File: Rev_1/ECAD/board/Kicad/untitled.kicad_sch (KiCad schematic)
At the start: 1 part

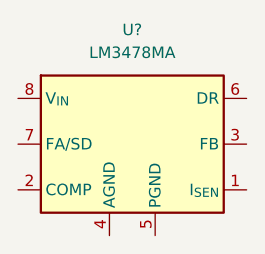
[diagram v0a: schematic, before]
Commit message: Moved Input Capacitors to minimize loop area and created pours for boost converter
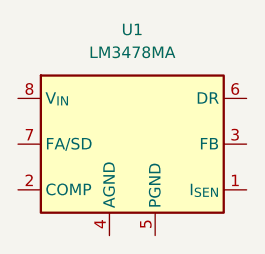
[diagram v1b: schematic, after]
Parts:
- gave numbers to parts that had none: 1
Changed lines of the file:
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@@
 		(dnp no)
 		(fields_autoplaced yes)
-		(property "Reference" "U?"
+		(property "Reference" "U1"
 			(at 64.77 38.1 0)
 			(effects
@@
 			(project ""
 				(path "/bb89802d-7e38-4fba-a75e-923c723cd6a1/ac666ba1-6694-41e5-b795-864ebc43cc42"
-					(reference "U?")
+					(reference "U1")
 					(unit 1)
 				)

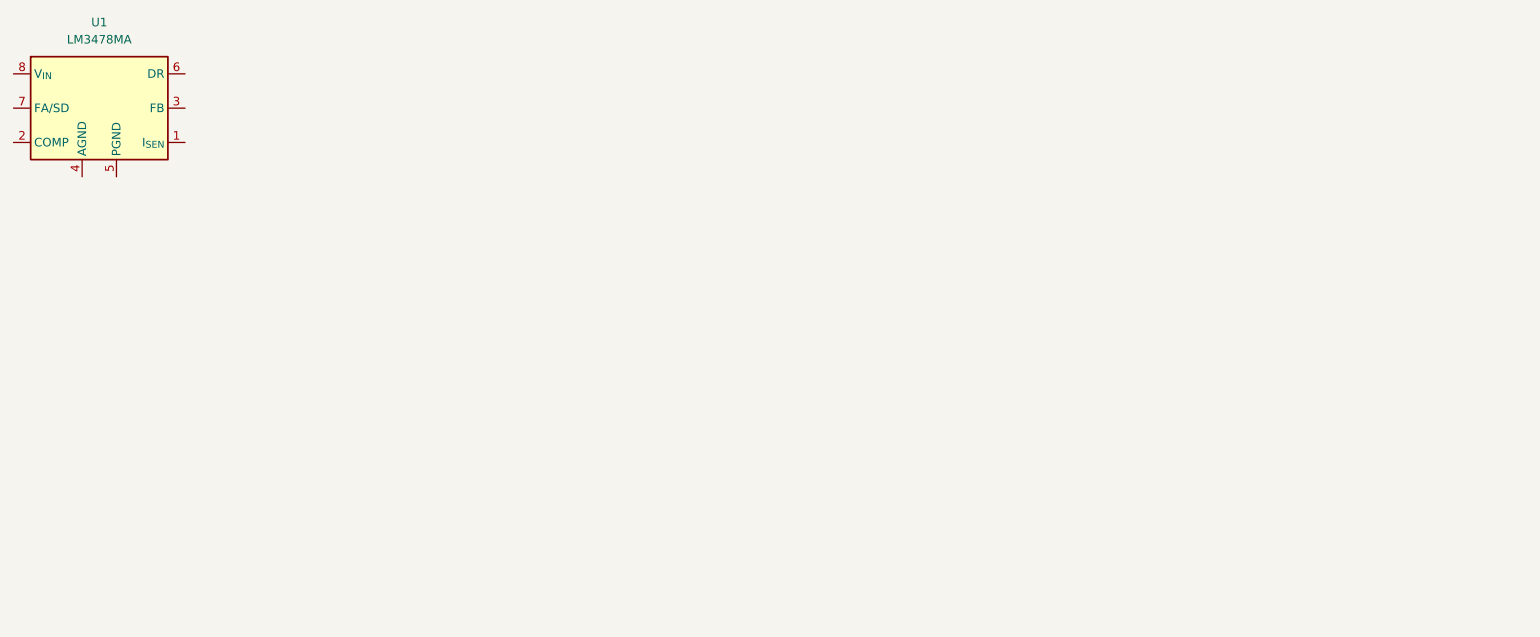
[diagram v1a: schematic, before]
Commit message: Added inverted buck-boost for -17V rail
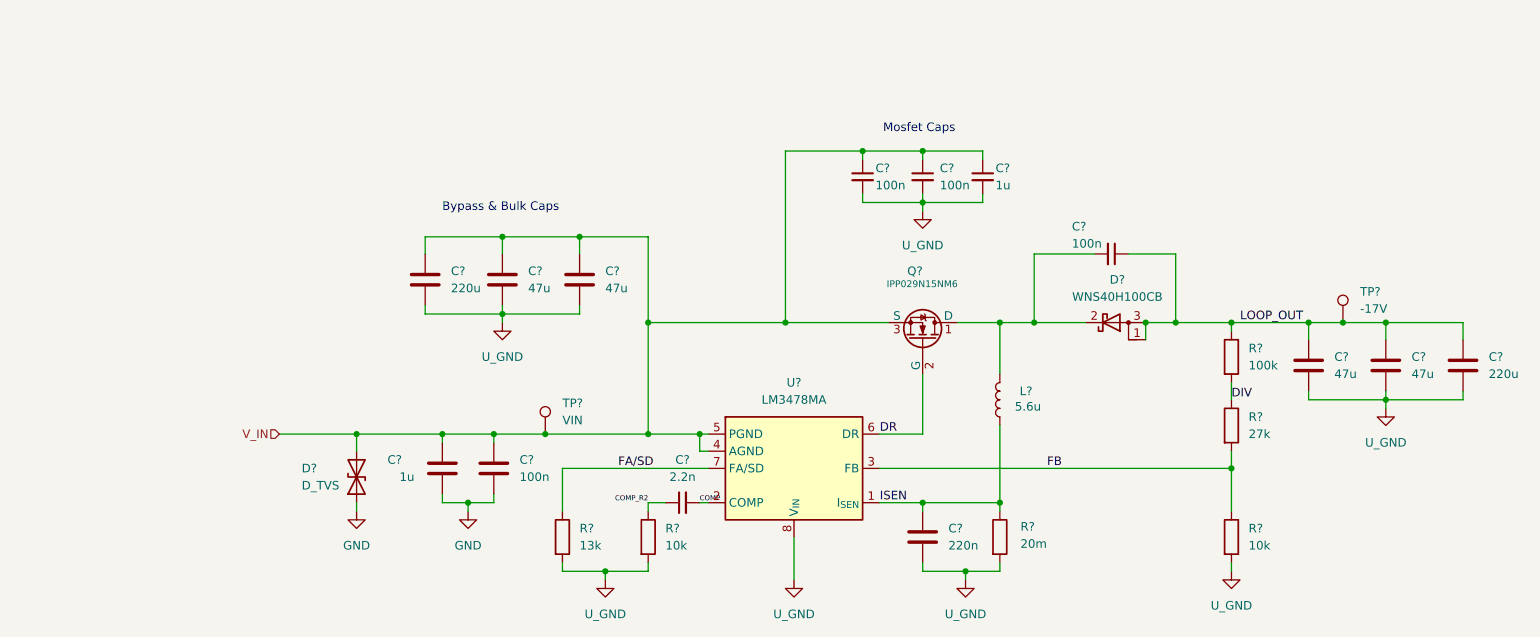
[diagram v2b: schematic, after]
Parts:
- removed U1: LM3478MA, Package_SO:SOIC-8_3.9x4.9mm_P1.27mm, symbol Regulator_Controller:LM3478MA
- added C?: 220n, Capacitor_SMD:C_0603_1608Metric_Pad1.08x0.95mm_HandSolder, symbol Device:C
- added C? (x2): 220u, Capacitor_SMD:CP_Elec_10x10.5, symbol Device:C
- added C? (x4): 47u, Capacitor_SMD:C_1210_3225Metric_Pad1.33x2.70mm_HandSolder, symbol Device:C
- added C? (x3): 100n, Capacitor_SMD:C_0603_1608Metric_Pad1.08x0.95mm_HandSolder, symbol Device:C_Small
- added C?: 1u, Capacitor_SMD:C_0603_1608Metric_Pad1.08x0.95mm_HandSolder, symbol Device:C_Small
- added C?: 1u, Capacitor_SMD:C_0603_1608Metric_Pad1.08x0.95mm_HandSolder, symbol Device:C
- added C?: 100n, Capacitor_SMD:C_0603_1608Metric_Pad1.08x0.95mm_HandSolder, symbol Device:C
- added C?: 2.2n, Capacitor_SMD:C_0603_1608Metric_Pad1.08x0.95mm_HandSolder, symbol Device:C_Small
- added D?: WNS40H100CB, Package_TO_SOT_THT:TO-220-3_Vertical, symbol Device:D_Schottky_AKA
- added D?: D_TVS, Diode_SMD:D_0805_2012Metric_Pad1.15x1.40mm_HandSolder, symbol Device:D_TVS
- added L?: 5.6u, filip:L_IHLP5050FD_5.0x5.0mm_Shielded, symbol Device:L
- added Q?: IPP029N15NM6, filip:TO-263-4_TabPin1-HandSoldered, symbol Simulation_SPICE:NMOS
- added R?: 27k, Resistor_SMD:R_0603_1608Metric_Pad0.98x0.95mm_HandSolder, symbol Device:R
- added R?: 100k, Resistor_SMD:R_0805_2012Metric_Pad1.20x1.40mm_HandSolder, symbol Device:R
- added R? (x2): 10k, Resistor_SMD:R_0805_2012Metric_Pad1.20x1.40mm_HandSolder, symbol Device:R
- added R?: 20m, Resistor_SMD:R_1206_3216Metric_Pad1.30x1.75mm_HandSolder, symbol Device:R
- added R?: 13k, Resistor_SMD:R_0603_1608Metric_Pad0.98x0.95mm_HandSolder, symbol Device:R
- added TP?: VIN, Connector_Pin:Pin_D0.7mm_L6.5mm_W1.8mm_FlatFork, symbol Connector:TestPoint
- added TP?: -17V, Connector_Pin:Pin_D0.7mm_L6.5mm_W1.8mm_FlatFork, symbol Connector:TestPoint
- added U?: LM3478MA, Package_SO:SOIC-8_3.9x4.9mm_P1.27mm, symbol Regulator_Controller:LM3478MA
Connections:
- new net: C?.2, D?.2 (K), L?.1, Q?.1 (D)
- new net COMP: C?.2, U?.2 (COMP)
- new net COMP_R2: C?.1, R?.1
- new net DIV: R?.1, R?.2
- new net DR: Q?.2 (G), U?.6 (DR)
- new net FA/SD: R?.1, U?.7 (FA/SD)
- new net FB: R?.1, R?.2, U?.3 (FB)
- new net GND: C?.2, C?.2, D?.1 (A1)
- new net ISEN: C?.1, L?.2, R?.1, U?.1 (I_{SEN})
- new net LOOP_OUT: C?.1, C?.1, C?.1, C?.1, D?.1 (A), D?.3 (A), R?.1, TP?.1
- new net U_GND: C?.2, C?.2, C?.2, C?.2, C?.2, C?.2, C?.2, C?.2, C?.2, C?.2, R?.2, R?.2, R?.2, R?.2, U?.8 (V_{IN})
- new net V_IN: C?.1, C?.1, C?.1, C?.1, C?.1, C?.1, C?.1, C?.1, D?.2 (A2), Q?.3 (S), TP?.1, U?.4 (AGND), U?.5 (PGND)
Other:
- note added: "Bypass & Bulk Caps"
- note added: "Mosfet Caps"

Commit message: Added Heatsink to Transistors
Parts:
- added C19, C23: 100n, Capacitor_SMD:C_0603_1608Metric_Pad1.08x0.95mm_HandSolder, symbol Device:C_Small
- added C20: 1u, Capacitor_SMD:C_0805_2012Metric_Pad1.18x1.45mm_HandSolder, symbol Device:C_Small
- added C21: 100n, Capacitor_SMD:C_0603_1608Metric_Pad1.08x0.95mm_HandSolder, symbol Device:C
- added C22: 10p, Capacitor_SMD:C_0603_1608Metric_Pad1.08x0.95mm_HandSolder, symbol Device:C
- added C24: 100u, Capacitor_SMD:CP_Elec_10x10.5, symbol Device:C_Small
- added C25: 1u, Capacitor_SMD:C_0603_1608Metric_Pad1.08x0.95mm_HandSolder, symbol Device:C_Small
- added C26: 10u, Capacitor_SMD:C_0805_2012Metric_Pad1.18x1.45mm_HandSolder, symbol Device:C_Small
- added C27: 220u, Capacitor_SMD:CP_Elec_10x10.5, symbol Device:C_Small
- added D5: 5V6, Diode_SMD:D_0805_2012Metric_Pad1.15x1.40mm_HandSolder, symbol Device:D_Zener
- added FB1: 100, Inductor_SMD:L_0805_2012Metric_Pad1.15x1.40mm_HandSolder, symbol Device:FerriteBead_Small
- added Q3: NPN, Package_TO_SOT_SMD:SOT-223-3_TabPin2, symbol Simulation_SPICE:NPN
- added Q4: PNP, symbol Simulation_SPICE:PNP
- added Q5: NMOS, symbol Simulation_SPICE:NMOS
- added R31: 100k, Resistor_SMD:R_0805_2012Metric_Pad1.20x1.40mm_HandSolder, symbol Device:R
- added R32, R33: 10k, Resistor_SMD:R_0805_2012Metric_Pad1.20x1.40mm_HandSolder, symbol Device:R
- added R34: 10, Resistor_SMD:R_0805_2012Metric_Pad1.20x1.40mm_HandSolder, symbol Device:R
- added R35: 20m, Resistor_SMD:R_1206_3216Metric_Pad1.30x1.75mm_HandSolder, symbol Device:R
- added R36, R37: ?, Resistor_SMD:R_0603_1608Metric_Pad0.98x0.95mm_HandSolder, symbol Device:R
- added R38: 100, Resistor_SMD:R_0805_2012Metric_Pad1.20x1.40mm_HandSolder, symbol Device:R
- added RV1: 10k, filip:Potentiometer_SMD_Trimmer_PVG3_3.6x3, symbol Device:R_Potentiometer_Trim
- added TP3: VREF, Connector_Pin:Pin_D0.7mm_L6.5mm_W1.8mm_FlatFork, symbol Connector:TestPoint
- added TP4: -15V, Connector_Pin:Pin_D0.7mm_L6.5mm_W1.8mm_FlatFork, symbol Connector:TestPoint
- added U6: LM358, Package_SO:SOIC-8_3.9x4.9mm_P1.27mm, symbol Amplifier_Operational:LM358
- gave numbers to parts that had none: 27
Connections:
- net GND: now also C13.2, C16.2, C17.2, C18.2, C5.2, C8.2, C9.2, R25.2, R26.2, R27.2, R30.2, U1.8 (V_{IN}), C19.2, C20.2, C25.2, C26.2, C27.2, D5.1 (K), Q5.3 (S), R31.1, R37.2
- net LOOP_OUT: now also FB1.1
- net U_GND: now also C21.2, C23.2, C24.2, U6.8 (V+); no longer C13.2, C16.2, C17.2, C18.2, C5.2, C8.2, C9.2, R25.2, R26.2, R27.2, R30.2, U1.8 (V_{IN})
- new net: C22.1, R34.1, U6.1
- new net: Q3.1 (B), Q4.1 (C), R33.2
- new net: Q4.2 (B), R34.2
- new net: R36.1, RV1.2
- new net: Q5.2 (G), R38.2
- new net -15V: C25.1, C26.1, C27.1, Q5.1 (D), R35.2, RV1.1, TP4.1
- new net -17V: C20.1, C21.1, FB1.2, Q3.3 (E), R32.1, R33.1, U6.4 (V-)
- new net SHUNT_IN: C23.1, C24.1, Q3.2 (C), Q4.3 (E), R35.1
- new net SHUTDOWN: R38.1
- new net V_FB: C22.2, R36.2, R37.1, U6.2 (-)
- new net V_REF: C19.1, D5.2 (A), R31.2, R32.2, TP3.1, U6.3 (+)
- no-connect marks 0 -> 1
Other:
- note added: "5V logic N-MOS with low RDS_ON"
- note added: ">=100mA"
- note added: ">=5-6A"
- moved on the sheet: C10, C11, C12, C13, C14, C15, C16, C17, C18, C5, C6, C7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

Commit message: made sketch of cuk converter
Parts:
- added C28, C31: 220u, Capacitor_SMD:CP_Elec_10x10.5, symbol Device:C
- added C29, C32, C33, C34: 47u, Capacitor_SMD:C_1210_3225Metric_Pad1.33x2.70mm_HandSolder, symbol Device:C
- added C30: 100n, symbol Device:C
- added C36: 1u, Capacitor_SMD:C_0603_1608Metric_Pad1.08x0.95mm_HandSolder, symbol Device:C
- added C37: 100n, Capacitor_SMD:C_0603_1608Metric_Pad1.08x0.95mm_HandSolder, symbol Device:C
- added C40: 2.2n, Capacitor_SMD:C_0603_1608Metric_Pad1.08x0.95mm_HandSolder, symbol Device:C_Small
- added C43: 220n, Capacitor_SMD:C_0603_1608Metric_Pad1.08x0.95mm_HandSolder, symbol Device:C
- added D6: WNS40H100CB, Package_TO_SOT_THT:TO-220-3_Vertical, symbol Device:D_Schottky_AKA
- added D7: D_TVS, Diode_SMD:D_0805_2012Metric_Pad1.15x1.40mm_HandSolder, symbol Device:D_TVS
- added L2, L3: 6.8u, filip:L_IHLP5050FD_5.0x5.0mm_Shielded, symbol Device:L
- added Q6: IPP029N15NM6, filip:TO-263-4_TabPin1-HandSoldered, symbol Simulation_SPICE:NMOS
- added R39: 13k, Resistor_SMD:R_0603_1608Metric_Pad0.98x0.95mm_HandSolder, symbol Device:R
- added R40: 10k, Resistor_SMD:R_0805_2012Metric_Pad1.20x1.40mm_HandSolder, symbol Device:R
- added R41: 20m, Resistor_SMD:R_1206_3216Metric_Pad1.30x1.75mm_HandSolder, symbol Device:R
- added TP5: VIN, Connector_Pin:Pin_D0.7mm_L6.5mm_W1.8mm_FlatFork, symbol Connector:TestPoint
- added U7: LM3478MA, Package_SO:SOIC-8_3.9x4.9mm_P1.27mm, symbol Regulator_Controller:LM3478MA
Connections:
- net COMP: now also C40.2, U7.2 (COMP)
- net COMP_R2: now also C40.1, R40.1
- net DR: now also Q6.2 (G), U7.6 (DR)
- net FA/SD: now also R39.1, U7.7 (FA/SD)
- net FB: now also U7.3 (FB)
- net GND: now also C28.2, C29.2, C30.2, C34.2, C36.2, C37.2, C43.2, D6.2 (K), D7.1 (A1), R39.2, R40.2, R41.2, U7.8 (V_{IN})
- net ISEN: now also C43.1, Q6.1 (D), R41.1, U7.1 (I_{SEN})
- net V_IN: now also C36.1, C37.1, D7.2 (A2), L2.2, TP5.1, U7.4 (AGND), U7.5 (PGND)
- new net: C30.1, C31.1, C32.1, C33.1, D6.1 (A), D6.3 (A), L3.2
- new net: C31.2, C32.2, C33.2, L2.1, Q6.3 (S)
- new net: C28.1, C29.1, C34.1, L3.1

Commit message: -15V schematic is mostly complete
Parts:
- removed C10: 2.2n, Capacitor_SMD:C_0603_1608Metric_Pad1.08x0.95mm_HandSolder, symbol Device:C_Small
- removed C11, C12, C15: 100n, Capacitor_SMD:C_0603_1608Metric_Pad1.08x0.95mm_HandSolder, symbol Device:C_Small
- removed C13: 220n, Capacitor_SMD:C_0603_1608Metric_Pad1.08x0.95mm_HandSolder, symbol Device:C
- removed C14: 1u, Capacitor_SMD:C_0603_1608Metric_Pad1.08x0.95mm_HandSolder, symbol Device:C_Small
- removed C16, C17, C32, C33, C8, C9: 47u, Capacitor_SMD:C_1210_3225Metric_Pad1.33x2.70mm_HandSolder, symbol Device:C
- removed C18, C31, C5: 220u, Capacitor_SMD:CP_Elec_10x10.5, symbol Device:C
- removed C30: 100n, symbol Device:C
- removed C6: 1u, Capacitor_SMD:C_0603_1608Metric_Pad1.08x0.95mm_HandSolder, symbol Device:C
- removed C7: 100n, Capacitor_SMD:C_0603_1608Metric_Pad1.08x0.95mm_HandSolder, symbol Device:C
- removed D3: D_TVS, Diode_SMD:D_0805_2012Metric_Pad1.15x1.40mm_HandSolder, symbol Device:D_TVS
- removed D4: WNS40H100CB, Package_TO_SOT_THT:TO-220-3_Vertical, symbol Device:D_Schottky_AKA
- removed L1: 5.6u, filip:L_IHLP5050FD_5.0x5.0mm_Shielded, symbol Device:L
- removed Q2: IPP029N15NM6, filip:TO-263-4_TabPin1-HandSoldered, symbol Simulation_SPICE:NMOS
- removed R25: 13k, Resistor_SMD:R_0603_1608Metric_Pad0.98x0.95mm_HandSolder, symbol Device:R
- removed R26, R30: 10k, Resistor_SMD:R_0805_2012Metric_Pad1.20x1.40mm_HandSolder, symbol Device:R
- removed R27: 20m, Resistor_SMD:R_1206_3216Metric_Pad1.30x1.75mm_HandSolder, symbol Device:R
- removed R28: 100k, Resistor_SMD:R_0805_2012Metric_Pad1.20x1.40mm_HandSolder, symbol Device:R
- removed R29: 27k, Resistor_SMD:R_0603_1608Metric_Pad0.98x0.95mm_HandSolder, symbol Device:R
- removed TP1: VIN, Connector_Pin:Pin_D0.7mm_L6.5mm_W1.8mm_FlatFork, symbol Connector:TestPoint
- removed TP2: -17V, Connector_Pin:Pin_D0.7mm_L6.5mm_W1.8mm_FlatFork, symbol Connector:TestPoint
- removed U1: LM3478MA, Package_SO:SOIC-8_3.9x4.9mm_P1.27mm, symbol Regulator_Controller:LM3478MA
- added C201: 220u, Capacitor_SMD:CP_Elec_10x10.5, symbol Device:C
- added C202, C203: 47u, Capacitor_SMD:C_1210_3225Metric_Pad1.33x2.70mm_HandSolder, symbol Device:C
- added C208: 56u, Capacitor_SMD:C_1210_3225Metric_Pad1.33x2.70mm_HandSolder, symbol Device:C
- added R204, R205: 1k, Resistor_SMD:R_0805_2012Metric_Pad1.20x1.40mm_HandSolder, symbol Device:R
- added R206: 100k, Resistor_SMD:R_0805_2012Metric_Pad1.20x1.40mm_HandSolder, symbol Device:R
- added R207: 27k, Resistor_SMD:R_0603_1608Metric_Pad0.98x0.95mm_HandSolder, symbol Device:R
- added R208: 10k, Resistor_SMD:R_0805_2012Metric_Pad1.20x1.40mm_HandSolder, symbol Device:R
- added TP105: -17V, Connector_Pin:Pin_D0.7mm_L6.5mm_W1.8mm_FlatFork, symbol Connector:TestPoint
- added U8: LM358, Package_SO:SOIC-8_3.9x4.9mm_P1.27mm, symbol Amplifier_Operational:LM358
- renumbered C36 to C204, C37 to C205, C40 to C206, C43 to C207, C34 to C209, C29 to C210, C28 to C211, C19 to C212, C20 to C213, C22 to C214, C23 to C215, C24 to C216, C21 to C217, C25 to C218, C26 to C219, C27 to C220, D7 to D201, D6 to D202, D5 to D203, L2 to L201, L3 to L202, Q6 to Q201, Q3 to Q202, Q4 to Q203, Q5 to Q205, R39 to R201, R40 to R202, R41 to R203, R31 to R209, R32 to R210, R33 to R211, R34 to R212, R35 to R213, R36 to R214, R37 to R215, R38 to R216, RV1 to RV201
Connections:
- net LOOP_OUT is gone; now on an unnamed net: FB1.1
- net DIV: now also R206.2, R207.1
- net GND: now also U7.4 (AGND), U7.5 (PGND), C201.2, C202.2, C203.2, R208.2, U8.3 (+); no longer U7.8 (V_{IN})
- net ISEN: now also Q201.3 (S); no longer Q201.1 (D)
- net V_IN: now also U7.8 (V_{IN}), C201.1, C202.1, C203.1; no longer U7.4 (AGND), U7.5 (PGND)
- net at D202.1 (A), D202.3 (A), L202.2: now also C208.2
- net at L201.1: now also Q201.1 (D), C208.1; no longer Q201.3 (S)
- net at C209.1, C210.1, C211.1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: now also R206.1, TP105.1
- net FB renamed FB_POSITIVE
- net FB_POSITIVE: now also R204.1, U8.1
- new net FB_NEGATIVE: R205.2, R207.2, R208.1
- new net FB_OP_NEG: R204.2, R205.1, U8.2 (-)
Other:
- note removed: "Mosfet Caps"
- moved on the sheet: C204, C205, C206, C207, C209, C210, C211, C212, C213, C214, C215, C216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
